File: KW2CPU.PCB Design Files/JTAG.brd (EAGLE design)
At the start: 160 x 100 mm, 2 parts

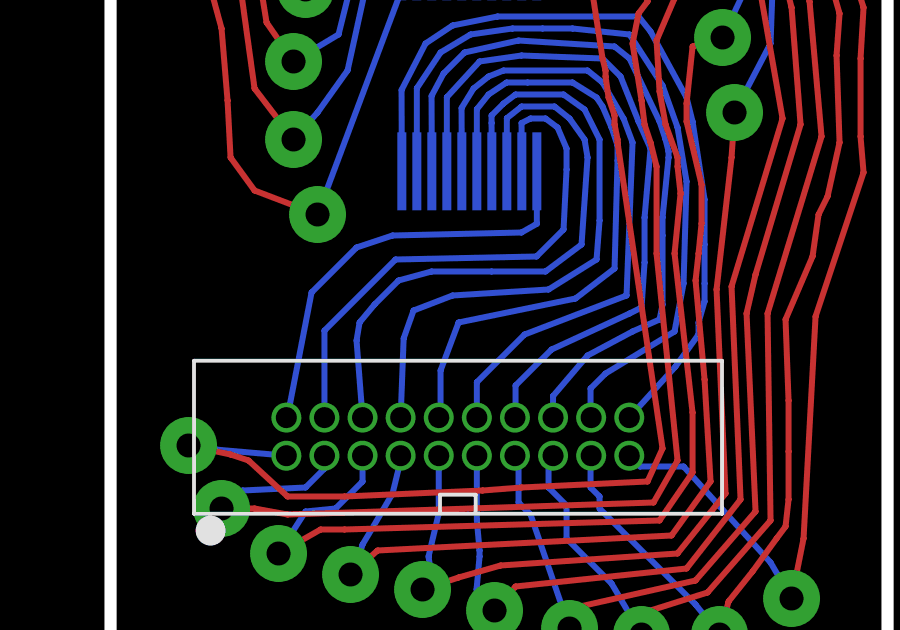
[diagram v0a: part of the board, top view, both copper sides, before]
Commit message: Added part numbers and manufacturers (inconsistent)
Also moved files to proper directories. Needs manual inconsistency
fixing
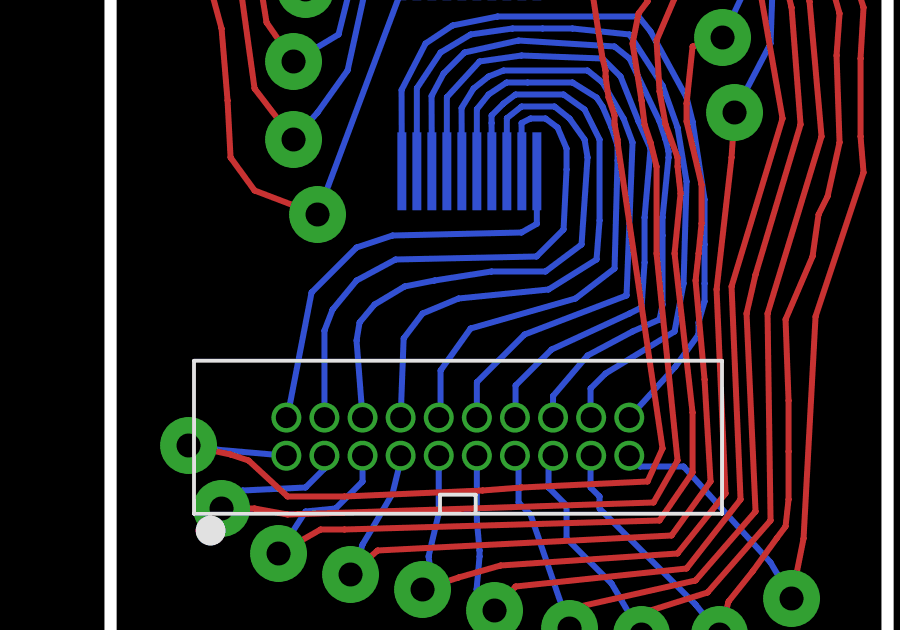
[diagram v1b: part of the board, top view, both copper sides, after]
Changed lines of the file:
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@@
 <wire x1="61.5" y1="23.2" x2="60.5" y2="23.2" width="0.4064" layer="20"/>
 <wire x1="60.5" y1="23.2" x2="60.5" y2="53" width="0.4064" layer="20"/>
-<dimension x1="60.5" y1="53" x2="86.4" y2="47.3" x3="73.45" y3="56.2" textsize="1.778" layer="20" dtype="horizontal"/>
-<dimension x1="60.5" y1="53" x2="66" y2="23.1" x3="52.8" y3="38.05" textsize="1.778" layer="20" dtype="vertical"/>
 </plain>
 <attributes>
@@
 </autorouter>
 <elements>
-<element name="U$1" library="KW2" package="MOLEX054722-0304" value="MOLEX54722-0304" x="72.46" y="43.74" rot="MR180"/>
+<element name="U$1" library="KW2" package="MOLEX054722-0304" value="MOLEX54722-0304" x="72.46" y="43.74" rot="MR180">
+<attribute name="MFGN" value="MOLEX" x="72.46" y="43.74" size="1.778" layer="28" rot="MR180" display="off"/>
+<attribute name="MFGP" value="54722-0304" x="72.46" y="43.74" size="1.778" layer="28" rot="MR180" display="off"/>
+</element>
 <element name="U$2" library="KW2" package="2X10JTAG" value="2X10JTAG" x="72.71" y="32.03"/>
 </elements>
@@
 <wire x1="77.4" y1="40.6" x2="77.3" y2="37" width="0.2" layer="16"/>
 <wire x1="77.3" y1="37" x2="76" y2="36" width="0.2" layer="16"/>
-<wire x1="76" y1="36" x2="72.1" y2="35.2" width="0.2" layer="16"/>
-<wire x1="72.1" y1="35.2" x2="71.5" y2="33.6" width="0.2" layer="16"/>
+<wire x1="76" y1="36" x2="72.5" y2="35" width="0.2" layer="16"/>
+<wire x1="72.5" y1="35" x2="71.5" y2="33.6" width="0.2" layer="16"/>
 <wire x1="71.5" y1="33.6" x2="71.5" y2="32.09" width="0.2" layer="16"/>
 <wire x1="71.5" y1="32.09" x2="71.44" y2="32.03" width="0.2" layer="16"/>
@@
 <contactref element="U$2" pad="P$8"/>
 <wire x1="70.17" y1="32.03" x2="70.27" y2="34.67" width="0.2" layer="16"/>
-<wire x1="70.27" y1="34.67" x2="70.6" y2="35.6" width="0.2" layer="16"/>
-<wire x1="70.6" y1="35.6" x2="71.9" y2="36.1" width="0.2" layer="16"/>
-<wire x1="71.9" y1="36.1" x2="75.1" y2="36.3" width="0.2" layer="16"/>
+<wire x1="70.27" y1="34.67" x2="70.9" y2="35.5" width="0.2" layer="16"/>
+<wire x1="70.9" y1="35.5" x2="72.1" y2="36" width="0.2" layer="16"/>
+<wire x1="72.1" y1="36" x2="75.1" y2="36.3" width="0.2" layer="16"/>
 <wire x1="75.1" y1="36.3" x2="76.7" y2="37.3" width="0.2" layer="16"/>
 <wire x1="76.7" y1="37.3" x2="76.8" y2="38.6" width="0.2" layer="16"/>
@@
 <wire x1="76.2" y1="37.8" x2="75" y2="36.9" width="0.2" layer="16"/>
 <wire x1="75" y1="36.9" x2="73.2" y2="36.9" width="0.2" layer="16"/>
-<wire x1="73.2" y1="36.9" x2="71.2" y2="36.9" width="0.2" layer="16"/>
-<wire x1="71.2" y1="36.9" x2="70.1" y2="36.6" width="0.2" layer="16"/>
-<wire x1="70.1" y1="36.6" x2="69.3" y2="35.8" width="0.2" layer="16"/>
+<wire x1="73.2" y1="36.9" x2="71.3" y2="36.6" width="0.2" layer="16"/>
+<wire x1="71.3" y1="36.6" x2="70.3" y2="36.4" width="0.2" layer="16"/>
+<wire x1="70.3" y1="36.4" x2="69.3" y2="35.8" width="0.2" layer="16"/>
 <wire x1="69.3" y1="35.8" x2="68.8" y2="35.2" width="0.2" layer="16"/>
 <wire x1="68.8" y1="35.2" x2="68.7" y2="34.6" width="0.2" layer="16"/>
@@
 <contactref element="U$1" pad="P$4"/>
 <wire x1="67.63" y1="32.03" x2="67.63" y2="34.93" width="0.2" layer="16"/>
-<wire x1="67.63" y1="34.93" x2="70" y2="37.3" width="0.2" layer="16"/>
+<wire x1="67.63" y1="34.93" x2="67.9" y2="35.63" width="0.2" layer="16"/>
+<wire x1="67.9" y1="35.63" x2="68.7" y2="36.6" width="0.2" layer="16"/>
+<wire x1="68.7" y1="36.6" x2="70" y2="37.3" width="0.2" layer="16"/>
 <wire x1="70" y1="37.3" x2="74.7" y2="37.4" width="0.2" layer="16"/>
 <wire x1="74.7" y1="37.4" x2="75.6" y2="38.3" width="0.2" layer="16"/>
